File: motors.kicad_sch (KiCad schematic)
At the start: 12 parts, among them U8 DRV8874PWPR, U9 DRV8874PWPR

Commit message: Update placement
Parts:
- added C30 (x2), C32 (x2): 100n, Capacitor_SMD:C_0402_1005Metric, symbol Device:C_Small
- added C31 (x2): 22n, Capacitor_SMD:C_0402_1005Metric, symbol Device:C_Small
- added C33 (x2): 100u, Capacitor_SMD:C_0805_2012Metric, symbol Device:C_Polarized_Small
- added U9 (x2): DRV8874PWPR, Libraries:SOP65P640X120-17N, symbol DRV8874PWPR:DRV8874PWPR
- C26, C27, C28, C30, C31, C32: footprint Capacitor_SMD:C_0603_1608Metric -> Capacitor_SMD:C_0402_1005Metric
- C29, C33: footprint Capacitor_SMD:C_0603_1608Metric -> Capacitor_SMD:C_0805_2012Metric
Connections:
- net +36V: now also C30.1, C30.1, C32.1, C32.1, C33.1, C33.1, U9.11 (VM), U9.11 (VM)
- net +3V3: now also U9.3 (NSLEEP), U9.3 (NSLEEP)
- net GND: now also C32.2, C32.2, C33.2, C33.2, U9.15 (GND), U9.15 (GND), U9.16 (PMODE), U9.16 (PMODE), U9.7 (IMODE), U9.7 (IMODE), U9.9 (PGND), U9.9 (PGND)
- net MOTOR_VREF: now also U9.5 (VREF), U9.5 (VREF)
- new net: C30.2, U9.12 (VCP) (x2)
- new net: C31.2, U9.13 (CPH) (x2)
- new net: C31.1, U9.14 (CPL) (x2)
- new net MOTOR_3_DIRECTION: U9.2 (PH/IN2)
- new net MOTOR_3_OUT_1: U9.8 (OUT1)
- new net MOTOR_3_OUT_2: U9.10 (OUT2)
- new net MOTOR_3_PWM: U9.1 (EN/IN1)
- new net MOTOR_4_DIRECTION: U9.2 (PH/IN2)
- new net MOTOR_4_OUT_1: U9.8 (OUT1)
- new net MOTOR_4_OUT_2: U9.10 (OUT2)
- new net MOTOR_4_PWM: U9.1 (EN/IN1)
- no-connect marks 4 -> 8
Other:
- moved on the sheet: C26, C27, C28, C29, C30, C31, C32, C33, R10, R9, U8, U9

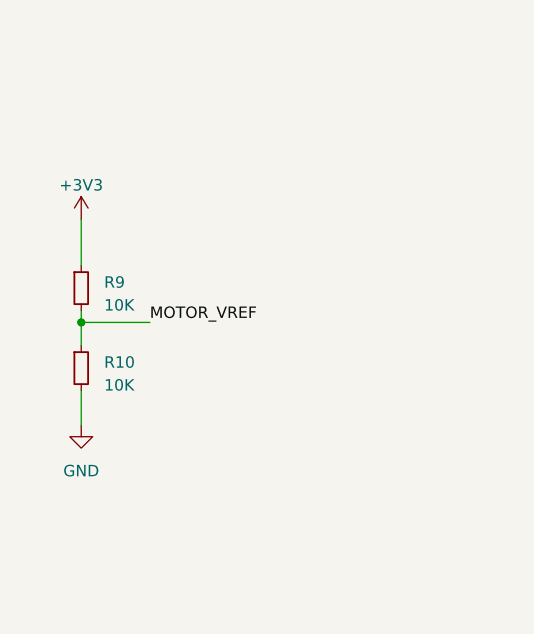
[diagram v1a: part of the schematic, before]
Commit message: route usb and flash
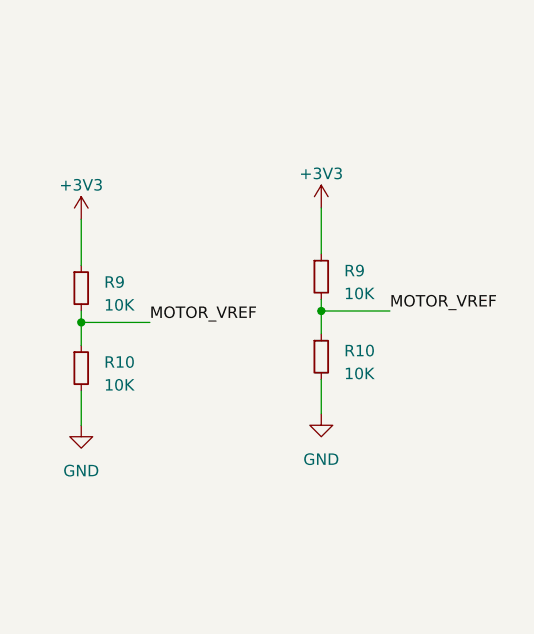
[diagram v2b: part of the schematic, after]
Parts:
- added R10, R9: 10K, Resistor_SMD:R_0603_1608Metric, symbol Device:R_Small
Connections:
- net +3V3: now also R9.1
- net GND: now also R10.2
- net MOTOR_VREF: now also R10.1, R9.2
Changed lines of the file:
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@@
   (junction (at 146.05 171.45) (diameter 0) (color 0 0 0 0)
+  )
+  (junction (at 381 139.7) (diameter 0) (color 0 0 0 0)
   )
   (junction (at 288.29 167.64) (diameter 0) (color 0 0 0 0)
@@
     (stroke (width 0) (type default))
   )
+  (wire (pts (xy 381 139.7) (xy 388.62 139.7))
+    (stroke (width 0) (type default))
+  )
   (wire (pts (xy 135.89 166.37) (xy 149.86 166.37))
     (stroke (width 0) (type default))
@@
     (stroke (width 0) (type default))
   )
+  (wire (pts (xy 381 138.43) (xy 381 139.7))
+    (stroke (width 0) (type default))
+  )
   (wire (pts (xy 311.15 102.87) (xy 311.15 104.14))
     (stroke (width 0) (type default))
@@
     (stroke (width 0) (type default))
   )
+  (wire (pts (xy 381 147.32) (xy 381 151.13))
+    (stroke (width 0) (type default))
+  )
   (wire (pts (xy 151.13 91.44) (xy 148.59 91.44))
     (stroke (width 0) (type default))
   )
+  (wire (pts (xy 381 139.7) (xy 381 142.24))
+    (stroke (width 0) (type default))
+  )
   (wire (pts (xy 242.57 177.8) (xy 236.22 177.8))
+    (stroke (width 0) (type default))
+  )
+  (wire (pts (xy 381 128.27) (xy 381 133.35))
     (stroke (width 0) (type default))
   )
@@
   (label "MOTOR_VREF" (at 232.41 185.42 180) (fields_autoplaced)
     (effects (font (size 1.27 1.27)) (justify right bottom))
+  )
+  (label "MOTOR_VREF" (at 388.62 139.7 0) (fields_autoplaced)
+    (effects (font (size 1.27 1.27)) (justify left bottom))
   )
   (label "MOTOR_VREF" (at 91.44 116.84 180) (fields_autoplaced)
@@
     )
   )
+  (symbol (lib_id "power:+3V3") (at 381 128.27 0) (unit 1)
+    (in_bom yes) (on_board yes) (dnp no) (fields_autoplaced)
+    (property "Reference" "#PWR039" (at 381 132.08 0)
+      (effects (font (size 1.27 1.27)) hide)
+    )
+    (property "Value" "+3V3" (at 381 124.46 0)
+      (effects (font (size 1.27 1.27)))
+    )
+    (property "Footprint" "" (at 381 128.27 0)
+      (effects (font (size 1.27 1.27)) hide)
+    )
+    (property "Datasheet" "" (at 381 128.27 0)
+      (effects (font (size 1.27 1.27)) hide)
+    )
+    (pin "1")
+    (instances
+      (project "RC-Car-Controller"
+        (path "/6532ed18-dd14-44a4-a4f8-6383f8135b66"
+          (reference "#PWR039") (unit 1)
+        )
+        (path "/6532ed18-dd14-44a4-a4f8-6383f8135b66/e7259fa7-f322-44a4-a973-0690db2883d4"
+          (reference "#PWR072") (unit 1)
+        )
+      )
+    )
+  )
+  (symbol (lib_id "power:GND") (at 381 151.13 0) (unit 1)
+    (in_bom yes) (on_board yes) (dnp no) (fields_autoplaced)
+    (property "Reference" "#PWR040" (at 381 157.48 0)
+      (effects (font (size 1.27 1.27)) hide)
+    )
+    (property "Value" "GND" (at 381 156.21 0)
+      (effects (font (size 1.27 1.27)))
+    )
+    (property "Footprint" "" (at 381 151.13 0)
+      (effects (font (size 1.27 1.27)) hide)
+    )
+    (property "Datasheet" "" (at 381 151.13 0)
+      (effects (font (size 1.27 1.27)) hide)
+    )
+    (pin "1")
+    (instances
+      (project "RC-Car-Controller"
+        (path "/6532ed18-dd14-44a4-a4f8-6383f8135b66"
+          (reference "#PWR040") (unit 1)
+        )
+        (path "/6532ed18-dd14-44a4-a4f8-6383f8135b66/e7259fa7-f322-44a4-a973-0690db2883d4"
+          (reference "#PWR073") (unit 1)
+        )
+      )
+    )
+  )
   (symbol (lib_id "Device:C_Polarized_Small") (at 311.15 171.45 0) (unit 1)
     (in_bom yes) (on_board yes) (dnp no) (fields_autoplaced)
@@
         (path "/6532ed18-dd14-44a4-a4f8-6383f8135b66/e7259fa7-f322-44a4-a973-0690db2883d4"
           (reference "#PWR054") (unit 1)
+        )
+      )
+    )
+  )
+  (symbol (lib_id "Device:R_Small") (at 381 135.89 0) (unit 1)
+    (in_bom yes) (on_board yes) (dnp no) (fields_autoplaced)
+    (property "Reference" "R9" (at 383.54 135.255 0)
+      (effects (font (size 1.27 1.27)) (justify left))
+    )
+    (property "Value" "10K" (at 383.54 137.795 0)
+      (effects (font (size 1.27 1.27)) (justify left))
+    )
+    (property "Footprint" "Resistor_SMD:R_0603_1608Metric" (at 381 135.89 0)
+      (effects (font (size 1.27 1.27)) hide)
+    )
+    (property "Datasheet" "~" (at 381 135.89 0)
+      (effects (font (size 1.27 1.27)) hide)
+    )
+    (pin "1")
+    (pin "2")
+    (instances
+      (project "RC-Car-Controller"
+        (path "/6532ed18-dd14-44a4-a4f8-6383f8135b66"
+          (reference "R9") (unit 1)
+        )
+        (path "/6532ed18-dd14-44a4-a4f8-6383f8135b66/e7259fa7-f322-44a4-a973-0690db2883d4"
+          (reference "R5") (unit 1)
         )
       )
@@
         )
       )
+    )
+  )
+  (symbol (lib_id "Device:R_Small") (at 381 144.78 0) (unit 1)
+    (in_bom yes) (on_board yes) (dnp no) (fields_autoplaced)
+    (property "Reference" "R10" (at 383.54 144.145 0)
+      (effects (font (size 1.27 1.27)) (justify left))
+    )
+    (property "Value" "10K" (at 383.54 146.685 0)
+      (effects (font (size 1.27 1.27)) (justify left))
+    )
+    (property "Footprint" "Resistor_SMD:R_0603_1608Metric" (at 381 144.78 0)
+      (effects (font (size 1.27 1.27)) hide)
+    )
+    (property "Datasheet" "~" (at 381 144.78 0)
+      (effects (font (size 1.27 1.27)) hide)
+    )
+    (pin "1")
+    (pin "2")
+    (instances
+      (project "RC-Car-Controller"
+        (path "/6532ed18-dd14-44a4-a4f8-6383f8135b66"
+          (reference "R10") (unit 1)
+        )
+        (path "/6532ed18-dd14-44a4-a4f8-6383f8135b66/e7259fa7-f322-44a4-a973-0690db2883d4"
+          (reference "R6") (unit 1)
+        )
+      )

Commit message: route motors
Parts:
- renumbered C31 to C11, C30 to C12, C32 to C13, C33 to C14, C31 to C17, C30 to C18, C32 to C35, C31 to C36, C30 to C37, C32 to C38, C33 to C39, C27 to C40, C26 to C41, C28 to C42, C29 to C43, C33 to C44, R9 to R14, R10 to R15, R9 to R5, R10 to R6, U8 to U10, U9 to U11, U9 to U5

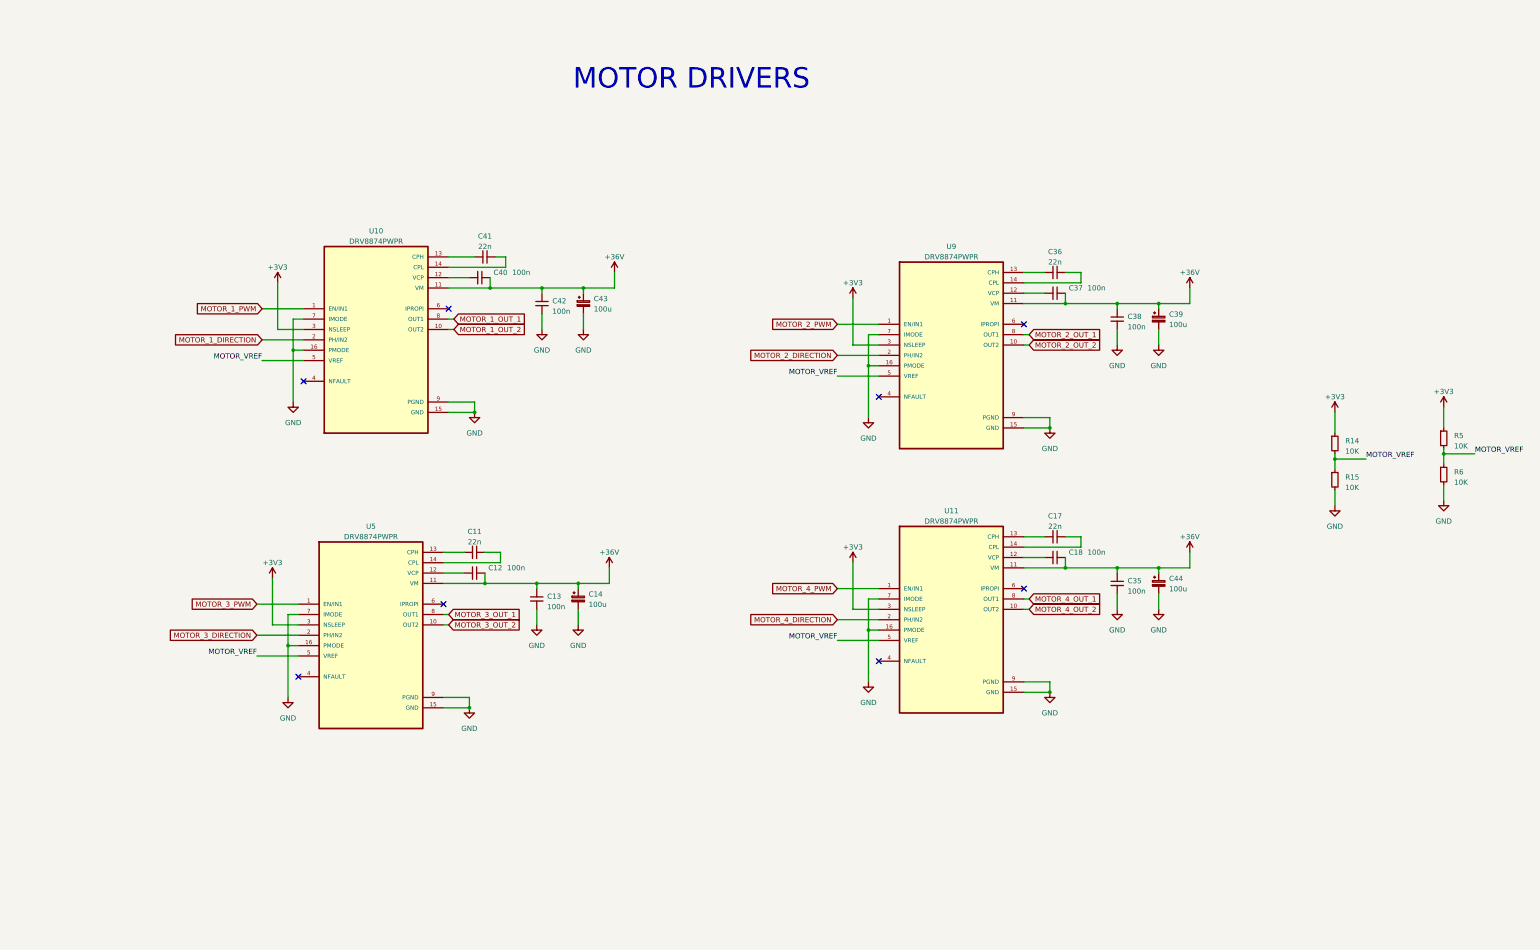
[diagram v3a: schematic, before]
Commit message: Add MPU6050 and LIS2MDL
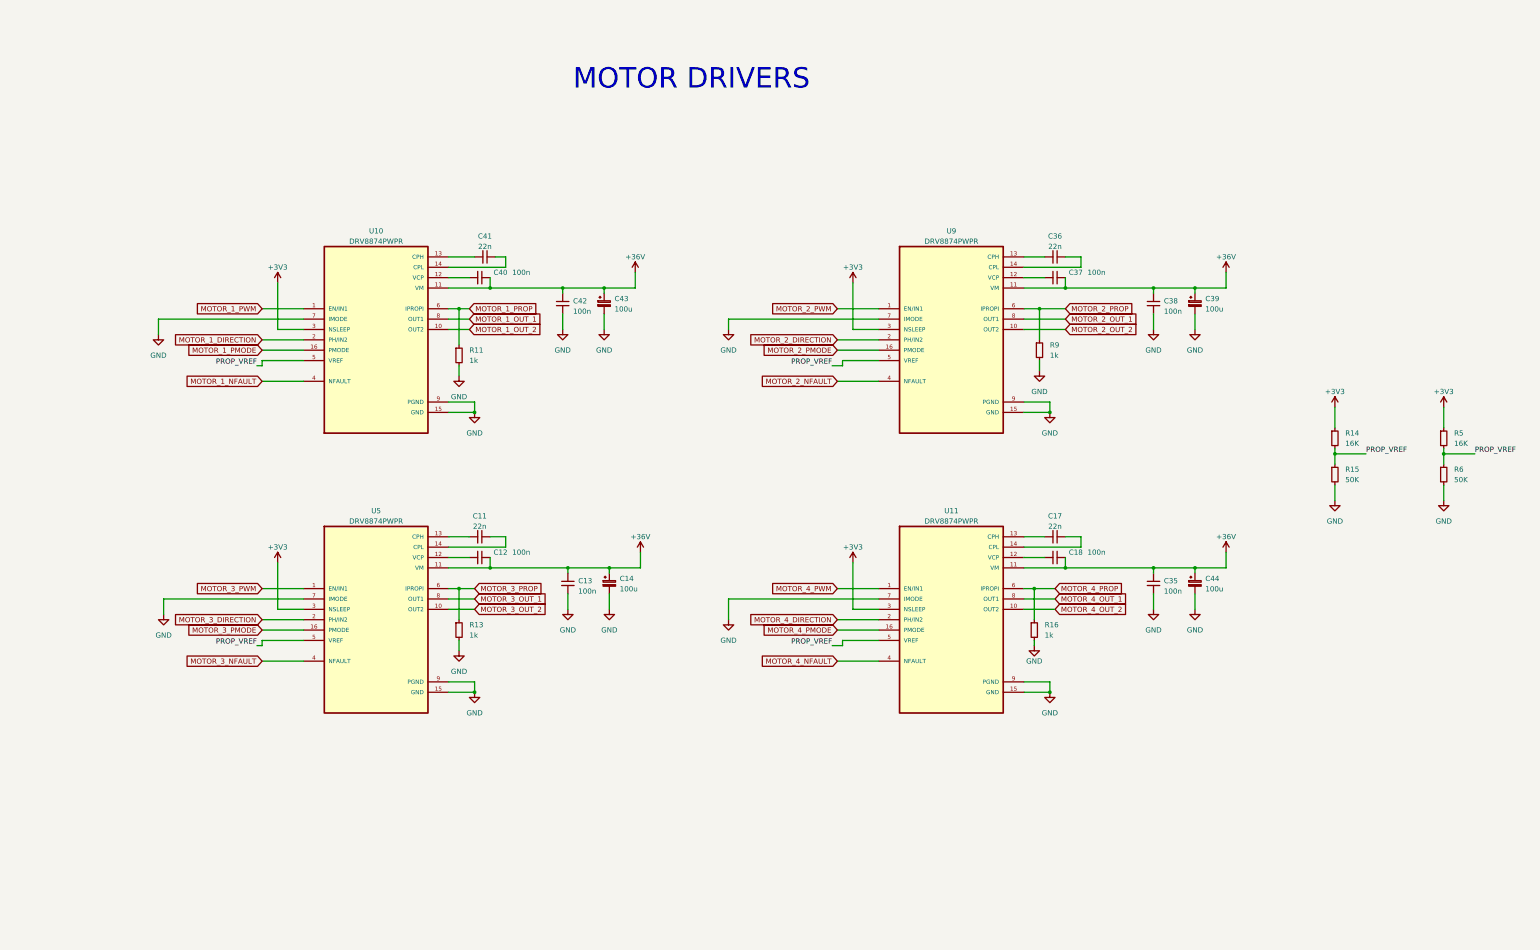
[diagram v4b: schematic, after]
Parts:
- added R11, R13, R16, R9: 1k, Resistor_SMD:R_0402_1005Metric, symbol Device:R_Small
- C11, C17, C36, C41: footprint Capacitor_SMD:C_0402_1005Metric -> Capacitor_SMD:C_0603_1608Metric; LCSC (none) -> C561176
- C14, C39, C43, C44: footprint Capacitor_SMD:C_0805_2012Metric -> Capacitor_SMD:CP_Elec_6.3x7.7
- R14, R5: value 10K -> 16K
- R15, R6: value 10K -> 50K
- U10, U11, U5, U9: Availability In Stock -> (none); Check_prices https://www.snapeda.com/parts/DRV8874PWPR/Texas+Instruments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 -> (none); LCSC (none) -> C1855818; MF Texas Instruments -> (none); MP DRV8874PWPR -> (none); Package HTSSOP-16 Texas Instruments -> (none); Price None -> (none); Purchase-URL https://www.snapeda.com/api/url_track_click_mouser/?unipart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 -> (none); SnapEDA_Link https://www.snapeda.com/parts/DRV8874PWPR/Texas+Instruments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 -> (none)
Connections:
- net GND: now also R11.2, R13.2, R16.2, R9.2; no longer U10.16 (PMODE), U11.16 (PMODE), U5.16 (PMODE), U9.16 (PMODE)
- net MOTOR_3_NFAULT: now reaches U5.4 (NFAULT)
- net MOTOR_3_PROP: now reaches U5.6 (IPROPI)
- net MOTOR_3_PROP: now also R13.1
- net MOTOR_1_NFAULT: now reaches U10.4 (NFAULT)
- net MOTOR_1_PROP: now reaches U10.6 (IPROPI)
- net MOTOR_1_PROP: now also R11.1
- net MOTOR_4_NFAULT: now reaches U11.4 (NFAULT)
- net MOTOR_4_PROP: now reaches U11.6 (IPROPI)
- net MOTOR_4_PROP: now also R16.1
- net MOTOR_2_NFAULT: now reaches U9.4 (NFAULT)
- net MOTOR_2_PROP: now reaches U9.6 (IPROPI)
- net MOTOR_2_PROP: now also R9.1
- net MOTOR_VREF renamed PROP_VREF
- new net MOTOR_1_PMODE: U10.16 (PMODE)
- new net MOTOR_2_PMODE: U9.16 (PMODE)
- new net MOTOR_3_PMODE: U5.16 (PMODE)
- new net MOTOR_4_PMODE: U11.16 (PMODE)
- no-connect marks 8 -> 0
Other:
- moved on the sheet: C11, C12, C13, C14, C35, C36, C37, C38, C39, C42, C43, C44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

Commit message: checkpoint for backup
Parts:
- added R19, R4: 16K, Resistor_SMD:R_0603_1608Metric, symbol Device:R_Small
- added R20, R7: 50K, Resistor_SMD:R_0603_1608Metric, symbol Device:R_Small
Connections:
- net MOTOR_2_NFAULT is gone; now on net MOTOR_NFAULT: U9.4 (NFAULT)
- net MOTOR_2_PMODE is gone; now on net MOTOR_PMODE: U9.16 (PMODE)
- net MOTOR_3_NFAULT is gone; now on net MOTOR_NFAULT: U5.4 (NFAULT)
- net MOTOR_3_PMODE is gone; now on net MOTOR_PMODE: U5.16 (PMODE)
- net MOTOR_4_NFAULT is gone; now on net MOTOR_NFAULT: U11.4 (NFAULT)
- net MOTOR_4_PMODE is gone; now on net MOTOR_PMODE: U11.16 (PMODE)
- net +3V3: now also R19.1, R4.1
- net GND: now also R20.2, R7.2
- net MOTOR_1_NFAULT renamed MOTOR_NFAULT
- net MOTOR_1_PMODE renamed MOTOR_PMODE
- removed net PROP_VREF: R14.2, R15.1, R5.2, R6.1, U10.5 (VREF), U11.5 (VREF), U5.5 (VREF), U9.5 (VREF)
- new net PROP_VREF_1: R14.2, R15.1, U10.5 (VREF)
- new net PROP_VREF_2: R5.2, R6.1, U9.5 (VREF)
- new net PROP_VREF_3: R4.2, R7.1, U5.5 (VREF)
- new net PROP_VREF_4: R19.2, R20.1, U11.5 (VREF)
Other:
- moved on the sheet: R14, R15, R5, R6

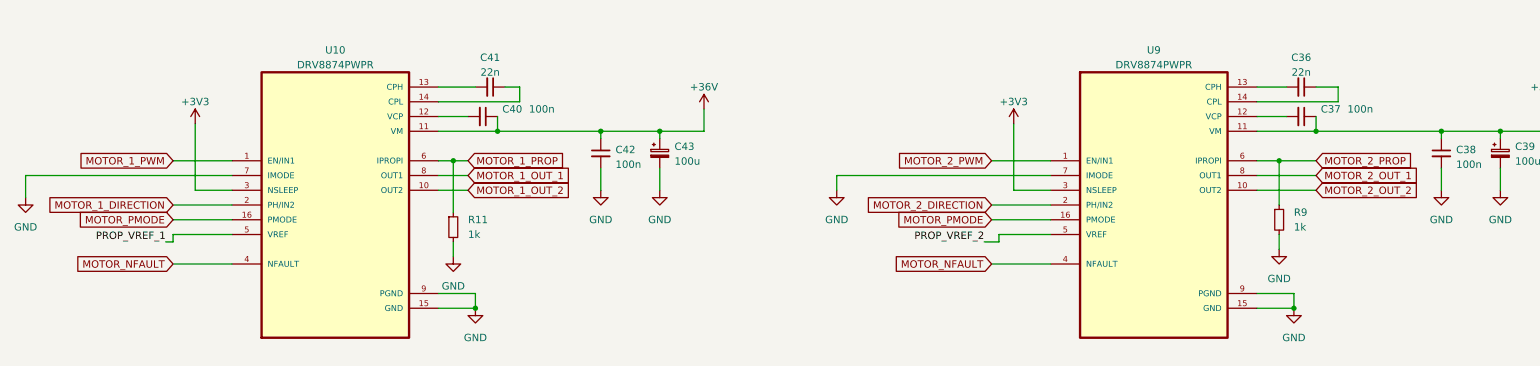
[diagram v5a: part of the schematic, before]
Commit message: Route Motor Drivers
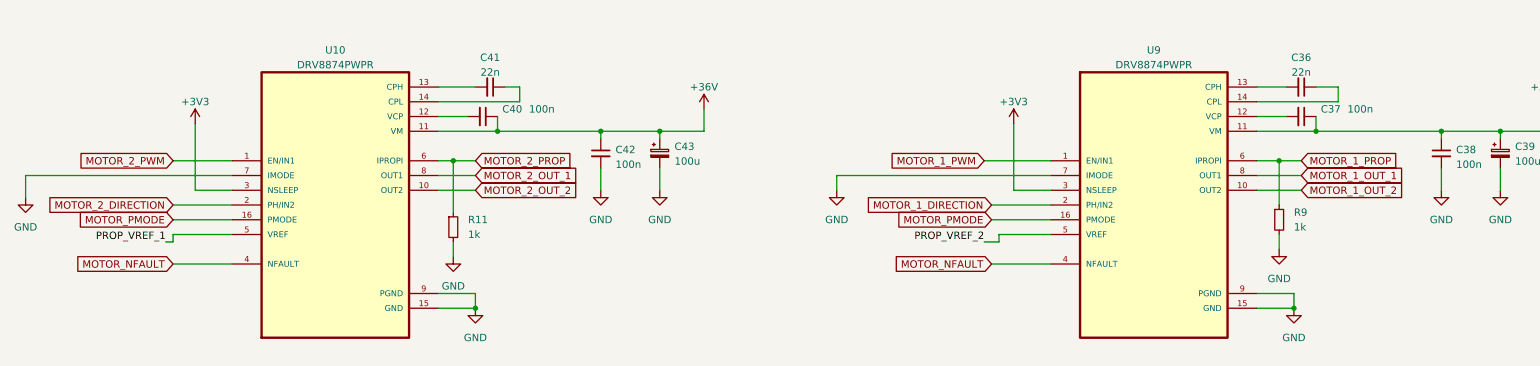
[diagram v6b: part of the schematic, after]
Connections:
- net MOTOR_1_DIRECTION: now also U9.2 (PH/IN2); no longer U10.2 (PH/IN2)
- net MOTOR_1_OUT_1: now also U9.8 (OUT1); no longer U10.8 (OUT1)
- net MOTOR_1_OUT_2: now also U9.10 (OUT2); no longer U10.10 (OUT2)
- net MOTOR_1_PROP: now also R9.1, U9.6 (IPROPI); no longer R11.1, U10.6 (IPROPI)
- net MOTOR_1_PWM: now also U9.1 (EN/IN1); no longer U10.1 (EN/IN1)
- net MOTOR_2_DIRECTION: now also U10.2 (PH/IN2); no longer U9.2 (PH/IN2)
- net MOTOR_2_OUT_1: now also U10.8 (OUT1); no longer U9.8 (OUT1)
- net MOTOR_2_OUT_2: now also U10.10 (OUT2); no longer U9.10 (OUT2)
- net MOTOR_2_PROP: now also R11.1, U10.6 (IPROPI); no longer R9.1, U9.6 (IPROPI)
- net MOTOR_2_PWM: now also U10.1 (EN/IN1); no longer U9.1 (EN/IN1)

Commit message: pcb updates & improvements
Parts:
- added R8: 16K, Resistor_SMD:R_0603_1608Metric, symbol Device:R_Small
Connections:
- net +3V3: now also R8.1
- net MOTOR_NFAULT: now also R8.2
- net PROP_VREF_1: now also U9.5 (VREF); no longer U10.5 (VREF)
- net PROP_VREF_2: now also U10.5 (VREF); no longer U9.5 (VREF)
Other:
- moved on the sheet: R14, R15, R19, R20, R4, R5, R6, R7
